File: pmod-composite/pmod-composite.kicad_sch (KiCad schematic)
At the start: 38 parts

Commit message: add many footprints
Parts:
- removed C?: 10u, symbol Device:C
- removed J? (x2): Conn_Coaxial, symbol Connector:Conn_Coaxial
- removed L? (x3): 1.8u, symbol Device:L
- removed L?: 2.2u, symbol Device:L
- added C?: 10u, Capacitor_THT:C_Disc_D3.0mm_W2.0mm_P2.50mm, symbol Device:C
- added J? (x2): PJRAN1X1U04X, SWITCHCRAFT_PJRAN1X1U04X, symbol PJRAN1X1U04X:PJRAN1X1U04X
- added L?: 2.2u, Inductor_THT:L_Axial_L5.3mm_D2.2mm_P10.16mm_Horizontal_Vishay_IM-1, symbol Device:L
- added L? (x3): 1.8u, Inductor_THT:L_Axial_L5.3mm_D2.2mm_P10.16mm_Horizontal_Vishay_IM-1, symbol Device:L
- C? (x4): footprint (none) -> Capacitor_THT:C_Disc_D5.0mm_W2.5mm_P2.50mm; DigikeyPart (none) -> FG28C0G1H271JNT06
- C?: footprint (none) -> Capacitor_THT:C_Disc_D3.0mm_W2.0mm_P2.50mm; DigikeyPart (none) -> FG18X5R1E106MRT06
- L?: footprint (none) -> Inductor_THT:L_Axial_L5.3mm_D2.2mm_P10.16mm_Horizontal_Vishay_IM-1; DigikeyPart (none) -> 78F2R2K-RC
- L?: footprint (none) -> Inductor_THT:L_Axial_L5.3mm_D2.2mm_P10.16mm_Horizontal_Vishay_IM-1; DigikeyPart (none) -> 78F1R8K-RC
- R? (x14): footprint (none) -> Resistor_THT:R_Axial_DIN0207_L6.3mm_D2.5mm_P7.62mm_Horizontal
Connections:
- net GND: now also J?.2, J?.2, J?.3, J?.3
- net at C?.1, L?.2: now also L?.1
- net at C?.1, C?.1: now also L?.2
- net at C?.1: now also C?.1, L?.2
- net at C?.2: now also J?.1
- net at C?.1: now also L?.1, L?.2 (x2)
- net at C?.1, R?.2: now also L?.1
- new net: C?.2, J?.1

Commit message: add connector footprint
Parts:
- J?: footprint (none) -> Connector_PinHeader_1.00mm:PinHeader_2x06_P1.00mm_Vertical
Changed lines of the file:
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@@
     (property "Reference" "J?" (id 0) (at 43.18 33.02 0))
     (property "Value" "Conn_02x06_Top_Bottom" (id 1) (at 43.18 35.56 0))
-    (property "Footprint" "" (id 2) (at 41.91 44.45 0)
+    (property "Footprint" "Connector_PinHeader_1.00mm:PinHeader_2x06_P1.00mm_Vertical" (id 2) (at 41.91 44.45 0)
       (effects (font (size 1.27 1.27)) hide)
     )
@@
     )
     (path "/e502d1d5-04b0-4d4b-b5c3-8c52d09668e7"
-      (reference "J?") (unit 1) (value "Conn_02x06_Top_Bottom") (footprint "")
+      (reference "J?") (unit 1) (value "Conn_02x06_Top_Bottom") (footprint "Connector_PinHeader_1.00mm:PinHeader_2x06_P1.00mm_Vertical")
     )
     (path "/34c6ac3a-bc5b-479f-b713-08da9a4d3801"

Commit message: work on PCB layout
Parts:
- C1, C2, C5, C6, C7, C8: renamed from C?; footprint (none) -> Capacitor_THT:C_Disc_D5.0mm_W2.5mm_P2.50mm
- J2: renamed from J?; footprint SWITCHCRAFT_PJRAN1X1U04X -> 00Project:SWITCHCRAFT_PJRAN1X1U04X
- gave numbers to parts that had none: 29

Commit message: route board
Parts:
- J1: footprint Connector_PinHeader_1.00mm:PinHeader_2x06_P1.00mm_Vertical -> 00Project:PMOD
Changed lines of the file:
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@@
     (property "Reference" "J1" (id 0) (at 43.18 33.02 0))
     (property "Value" "Conn_02x06_Top_Bottom" (id 1) (at 43.18 35.56 0))
-    (property "Footprint" "Connector_PinHeader_1.00mm:PinHeader_2x06_P1.00mm_Vertical" (id 2) (at 41.91 44.45 0)
+    (property "Footprint" "00Project:PMOD" (id 2) (at 41.91 44.45 0)
       (effects (font (size 1.27 1.27)) hide)
     )
@@
     )
     (path "/e502d1d5-04b0-4d4b-b5c3-8c52d09668e7"
-      (reference "J1") (unit 1) (value "Conn_02x06_Top_Bottom") (footprint "Connector_PinHeader_1.00mm:PinHeader_2x06_P1.00mm_Vertical")
+      (reference "J1") (unit 1) (value "Conn_02x06_Top_Bottom") (footprint "00Project:PMOD")
     )
     (path "/aed217f9-7149-4c90-ba0b-806c9d0d0e41"

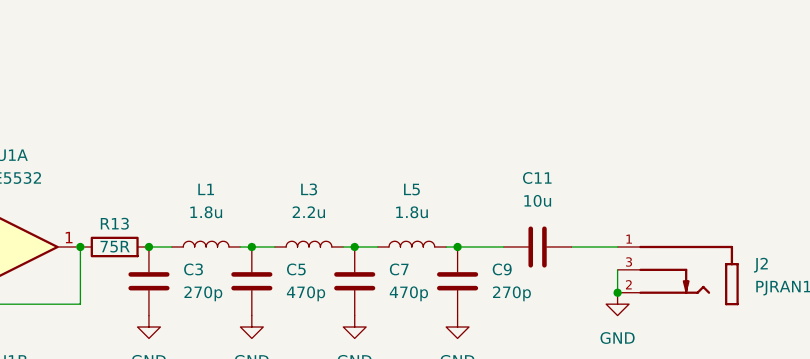
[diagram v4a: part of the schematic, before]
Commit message: relocate README.
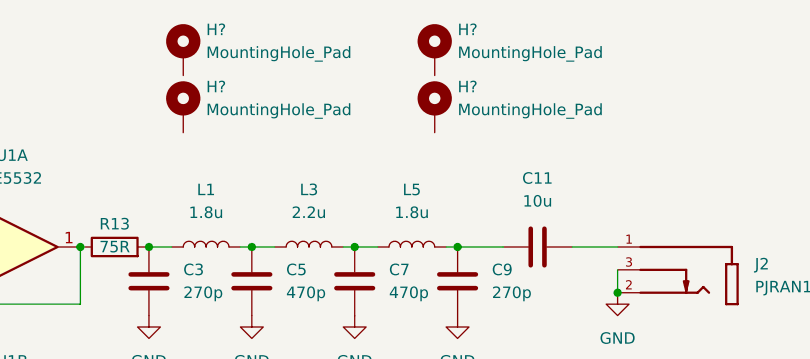
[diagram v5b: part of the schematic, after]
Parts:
- added H? (x4): MountingHole_Pad, MountingHole:MountingHole_3.2mm_M3_DIN965_Pad, symbol Mechanical:MountingHole_Pad
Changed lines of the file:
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@@
     (pin "2")
+  )
+  (symbol (lib_id "Mechanical:MountingHole_Pad") (at 148.59 20.32 0) (unit 1)
+    (in_bom yes) (on_board yes) (fields_autoplaced)
+    (property "Reference" "H?" (id 0) (at 151.13 17.7799 0)
+      (effects (font (size 1.27 1.27)) (justify left))
+    )
+    (property "Value" "MountingHole_Pad" (id 1) (at 151.13 20.3199 0)
+      (effects (font (size 1.27 1.27)) (justify left))
+    )
+    (property "Footprint" "MountingHole:MountingHole_3.2mm_M3_DIN965_Pad" (id 2) (at 148.59 20.32 0)
+      (effects (font (size 1.27 1.27)) hide)
+    )
+    (property "Datasheet" "~" (id 3) (at 148.59 20.32 0)
+      (effects (font (size 1.27 1.27)) hide)
+    )
+    (pin "1")
   )
   (symbol (lib_id "power:GND") (at 196.85 46.99 0) (unit 1)
@@
     (pin "2")
   )
+  (symbol (lib_id "Mechanical:MountingHole_Pad") (at 176.53 20.32 0) (unit 1)
+    (in_bom yes) (on_board yes) (fields_autoplaced)
+    (property "Reference" "H?" (id 0) (at 179.07 17.7799 0)
+      (effects (font (size 1.27 1.27)) (justify left))
+    )
+    (property "Value" "MountingHole_Pad" (id 1) (at 179.07 20.3199 0)
+      (effects (font (size 1.27 1.27)) (justify left))
+    )
+    (property "Footprint" "MountingHole:MountingHole_3.2mm_M3_DIN965_Pad" (id 2) (at 176.53 20.32 0)
+      (effects (font (size 1.27 1.27)) hide)
+    )
+    (property "Datasheet" "~" (id 3) (at 176.53 20.32 0)
+      (effects (font (size 1.27 1.27)) hide)
+    )
+    (pin "1")
+  )
   (symbol (lib_id "Device:C") (at 179.07 45.72 0) (unit 1)
     (in_bom yes) (on_board yes) (fields_autoplaced)
@@
     (pin "2")
     (pin "3")
+  )
+  (symbol (lib_id "Mechanical:MountingHole_Pad") (at 176.53 26.67 0) (unit 1)
+    (in_bom yes) (on_board yes) (fields_autoplaced)
+    (property "Reference" "H?" (id 0) (at 179.07 24.1299 0)
+      (effects (font (size 1.27 1.27)) (justify left))
+    )
+    (property "Value" "MountingHole_Pad" (id 1) (at 179.07 26.6699 0)
+      (effects (font (size 1.27 1.27)) (justify left))
+    )
+    (property "Footprint" "MountingHole:MountingHole_3.2mm_M3_DIN965_Pad" (id 2) (at 176.53 26.67 0)
+      (effects (font (size 1.27 1.27)) hide)
+    )
+    (property "Datasheet" "~" (id 3) (at 176.53 26.67 0)
+      (effects (font (size 1.27 1.27)) hide)
+    )
+    (pin "1")
   )
   (symbol (lib_id "Device:R") (at 92.71 54.61 90) (unit 1)
@@
     (pin "1")
   )
+  (symbol (lib_id "Mechanical:MountingHole_Pad") (at 148.59 26.67 0) (unit 1)
+    (in_bom yes) (on_board yes) (fields_autoplaced)
+    (property "Reference" "H?" (id 0) (at 151.13 24.1299 0)
+      (effects (font (size 1.27 1.27)) (justify left))
+    )
+    (property "Value" "MountingHole_Pad" (id 1) (at 151.13 26.6699 0)
+      (effects (font (size 1.27 1.27)) (justify left))
+    )
+    (property "Footprint" "MountingHole:MountingHole_3.2mm_M3_DIN965_Pad" (id 2) (at 148.59 26.67 0)
+      (effects (font (size 1.27 1.27)) hide)
+    )
+    (property "Datasheet" "~" (id 3) (at 148.59 26.67 0)
+      (effects (font (size 1.27 1.27)) hide)
+    )
+    (pin "1")
+  )
   (symbol (lib_id "power:GND") (at 167.64 72.39 0) (unit 1)
     (in_bom yes) (on_board yes) (fields_autoplaced)
@@
       (reference "C12") (unit 1) (value "10u") (footprint "Capacitor_THT:C_Disc_D3.0mm_W2.0mm_P2.50mm")
     )
+    (path "/4017294f-3b46-4bd3-b270-34a827f4594e"
+      (reference "H?") (unit 1) (value "MountingHole_Pad") (footprint "MountingHole:MountingHole_3.2mm_M3_DIN965_Pad")
+    )
+    (path "/9f60f0c7-2989-4ab1-bc00-3070593ad72e"
+      (reference "H?") (unit 1) (value "MountingHole_Pad") (footprint "MountingHole:MountingHole_3.2mm_M3_DIN965_Pad")
+    )
+    (path "/aeeeb7c6-b6eb-46bf-bb85-820ac4c1f9a1"
+      (reference "H?") (unit 1) (value "MountingHole_Pad") (footprint "MountingHole:MountingHole_3.2mm_M3_DIN965_Pad")
+    )
+    (path "/f04d7481-018d-4b3f-b8b8-d091ff23b8db"
+      (reference "H?") (unit 1) (value "MountingHole_Pad") (footprint "MountingHole:MountingHole_3.2mm_M3_DIN965_Pad")
+    )
     (path "/e502d1d5-04b0-4d4b-b5c3-8c52d09668e7"
